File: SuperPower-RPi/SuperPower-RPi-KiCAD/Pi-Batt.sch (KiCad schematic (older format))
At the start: 10 parts, among them J2 Conn_01x02, J4 Conn_01x02, Q1 SSM3J328R, Q6 Q_NMOS_GSD

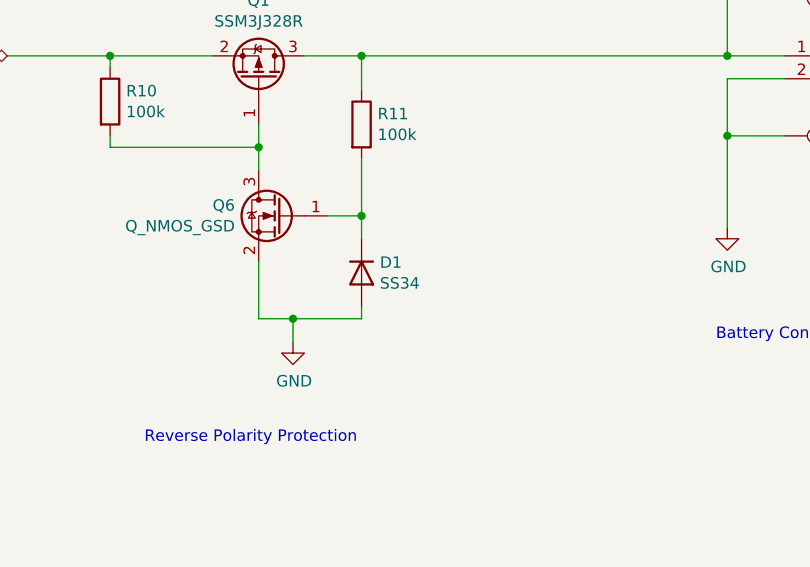
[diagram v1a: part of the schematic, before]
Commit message: Shrank Components and seleected NMOS part.
Shrank diodes to SOD523 and 100k resistors to 0402.
Selected 2N7002 for generic NMOS.
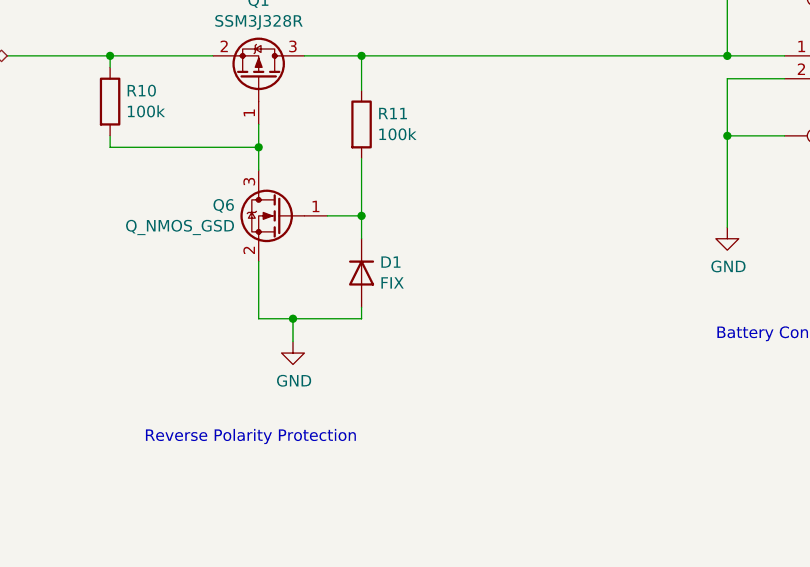
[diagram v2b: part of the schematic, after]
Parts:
- D1: value SS34 -> FIX; footprint Diode_SMD:D_SOD-123 -> Diode_SMD:D_SOD-523
- R10, R11: footprint Resistor_SMD:R_0603_1608Metric -> Resistor_SMD:R_0402_1005Metric; Digi-Key PN 311-100KHRCT-ND -> (none); Mfg Yageo -> (none); Mfg PN RC0603FR-07100KL -> (none)
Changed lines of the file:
@@
 P 6100 3350
 F 0 "D1" V 6054 3430 50  0000 L CNN
-F 1 "SS34" V 6145 3430 50  0000 L CNN
-F 2 "Diode_SMD:D_SOD-123" H 6100 3350 50  0001 C CNN
+F 1 "FIX" V 6145 3430 50  0000 L CNN
+F 2 "Diode_SMD:D_SOD-523" H 6100 3350 50  0001 C CNN
 F 3 "~" H 6100 3350 50  0001 C CNN
 F 4 "FIX FOOTPRINT" H 6100 3350 50  0001 C CNN "Mfg"
@@
 F 0 "R11" H 6170 2746 50  0000 L CNN
 F 1 "100k" H 6170 2655 50  0000 L CNN
-F 2 "Resistor_SMD:R_0603_1608Metric" V 6030 2700 50  0001 C CNN
+F 2 "Resistor_SMD:R_0402_1005Metric" V 6030 2700 50  0001 C CNN
 F 3 "~" H 6100 2700 50  0001 C CNN
-F 4 "311-100KHRCT-ND" H 6100 2700 50  0001 C CNN "Digi-Key PN"
-F 5 "Yageo" H 6100 2700 50  0001 C CNN "Mfg"
-F 6 "RC0603FR-07100KL" H 6100 2700 50  0001 C CNN "Mfg PN"
+F 4 "" H 6100 2700 50  0001 C CNN "Digi-Key PN"
+F 5 "" H 6100 2700 50  0001 C CNN "Mfg"
+F 6 "" H 6100 2700 50  0001 C CNN "Mfg PN"
 	1    6100 2700
 	1    0    0    -1
@@
 F 0 "R10" H 5070 2646 50  0000 L CNN
 F 1 "100k" H 5070 2555 50  0000 L CNN
-F 2 "Resistor_SMD:R_0603_1608Metric" V 4930 2600 50  0001 C CNN
+F 2 "Resistor_SMD:R_0402_1005Metric" V 4930 2600 50  0001 C CNN
 F 3 "~" H 5000 2600 50  0001 C CNN
-F 4 "311-100KHRCT-ND" H 5000 2600 50  0001 C CNN "Digi-Key PN"
-F 5 "Yageo" H 5000 2600 50  0001 C CNN "Mfg"
-F 6 "RC0603FR-07100KL" H 5000 2600 50  0001 C CNN "Mfg PN"
+F 4 "" H 5000 2600 50  0001 C CNN "Digi-Key PN"
+F 5 "" H 5000 2600 50  0001 C CNN "Mfg"
+F 6 "" H 5000 2600 50  0001 C CNN "Mfg PN"
 	1    5000 2600
 	1    0    0    -1

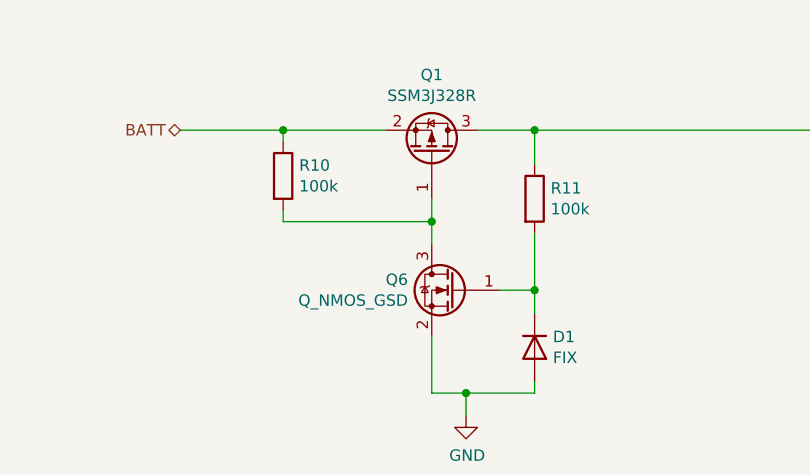
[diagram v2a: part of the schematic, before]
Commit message: Updated Component Meta-data
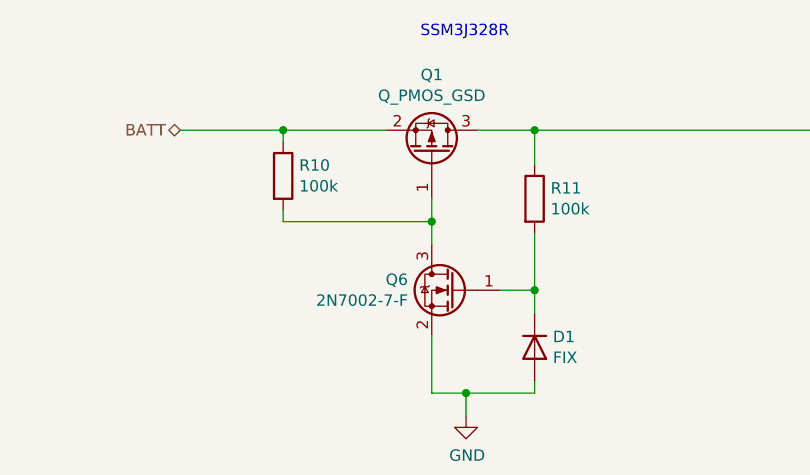
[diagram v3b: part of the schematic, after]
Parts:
- Q1: value SSM3J328R -> Q_PMOS_GSD
- Q6: value Q_NMOS_GSD -> 2N7002-7-F; Digi-Key PN (none) -> 2N7002-FDICT-ND; Mfg FIX FOOTPRINT -> Diodes Incorporated; Mfg PN (none) -> 2N7002-7-F
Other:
- note added: "SSM3J328R"
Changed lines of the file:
@@
 P 5650 2500
 F 0 "Q1" V 5992 2500 50  0000 C CNN
-F 1 "SSM3J328R" V 5901 2500 50  0000 C CNN
+F 1 "Q_PMOS_GSD" V 5901 2500 50  0000 C CNN
 F 2 "Package_TO_SOT_SMD:SOT-23" H 5850 2600 50  0001 C CNN
 F 3 "~" H 5650 2500 50  0001 C CNN
@@
 AR Path="/5F6AC644/5FA86C0C" Ref="Q6"  Part="1"
 F 0 "Q6" H 5954 3146 50  0000 L CNN
-F 1 "Q_NMOS_GSD" H 5954 3055 50  0000 L CNN
+F 1 "2N7002-7-F" H 5954 3055 50  0000 L CNN
 F 2 "Package_TO_SOT_SMD:SOT-23" H 5950 3200 50  0001 C CNN
 F 3 "~" H 5750 3100 50  0001 C CNN
-F 4 "FIX FOOTPRINT" H 5750 3100 50  0001 C CNN "Mfg"
+F 4 "Diodes Incorporated" H 5750 3100 50  0001 C CNN "Mfg"
+F 5 "2N7002-FDICT-ND" H 5750 3100 50  0001 C CNN "Digi-Key PN"
+F 6 "2N7002-7-F" H 5750 3100 50  0001 C CNN "Mfg PN"
 	1    5750 3100
 	-1   0    0    -1
@@
 Wire Wire Line
 	4100 6250 4100 6000
+Text Notes 5600 2000 0    50   ~ 0
+SSM3J328R
 $EndSCHEMATC

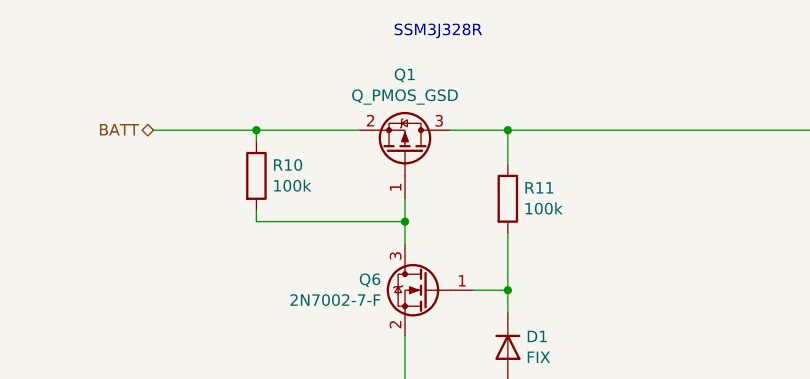
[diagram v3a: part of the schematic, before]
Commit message: Selected part for PMOS: DMP3056.
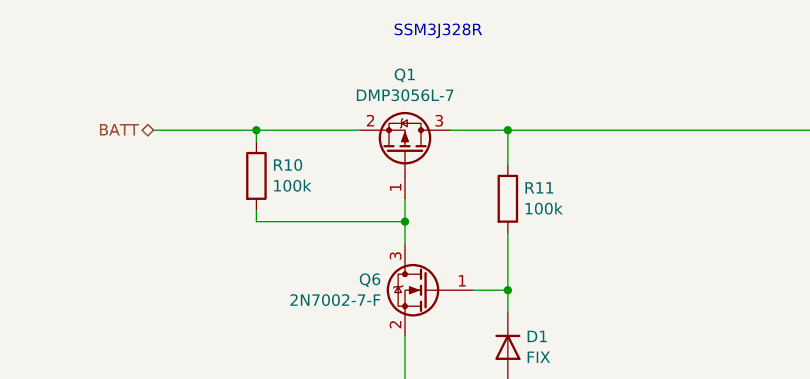
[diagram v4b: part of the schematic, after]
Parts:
- removed Q1: Q_PMOS_GSD, Package_TO_SOT_SMD:SOT-23, symbol Device:Q_PMOS_GSD
- added Q1: Q_PMOS_DMP3056L-7_SOT-23, Package_TO_SOT_SMD:SOT-23, symbol Manual_Lib:Q_PMOS_DMP3056L-7_SOT-23
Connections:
- net BATT: now also Q1.2 (S)
- net at J2.1 (Pin_1), R11.1, TP1.1: now also Q1.3 (D)
- net at Q6.3 (D), R10.2: now also Q1.1 (G)
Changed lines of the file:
@@
 	1    0    0    -1
-$EndComp
-$Comp
-L Device:Q_PMOS_GSD Q1
-U 1 1 5F704F9B
-P 5650 2500
-F 0 "Q1" V 5992 2500 50  0000 C CNN
-F 1 "Q_PMOS_GSD" V 5901 2500 50  0000 C CNN
-F 2 "Package_TO_SOT_SMD:SOT-23" H 5850 2600 50  0001 C CNN
-F 3 "~" H 5650 2500 50  0001 C CNN
-F 4 "FIX FOOTPRINT" H 5650 2500 50  0001 C CNN "Mfg"
-	1    5650 2500
-	0    1    -1   0
 $EndComp
 Wire Wire Line
@@
 Text Notes 5600 2000 0    50   ~ 0
 SSM3J328R
+$Comp
+L Manual_Lib:Q_PMOS_DMP3056L-7_SOT-23 Q1
+U 1 1 5FCC9BCC
+P 5650 2500
+F 0 "Q1" V 5992 2500 50  0000 C CNN
+F 1 "Q_PMOS_DMP3056L-7_SOT-23" H 5850 2450 50  0001 L CNN
+F 2 "Package_TO_SOT_SMD:SOT-23" H 5850 2600 50  0001 C CNN
+F 3 "https://www.diodes.com/assets/Datasheets/DMP3056L.pdf" H 5650 2500 50  0001 C CNN
+F 4 "Diodes Incorporated" H 5650 2500 50  0001 C CNN "Mfg"
+F 5 "DMP3056L-7" V 5901 2500 50  0000 C CNN "Mfg PN"
+F 6 "DMP3056L-7DICT-ND" H 5650 2500 50  0001 C CNN "Digi-Key PN"
+	1    5650 2500
+	0    1    -1   0
+$EndComp
 $EndSCHEMATC

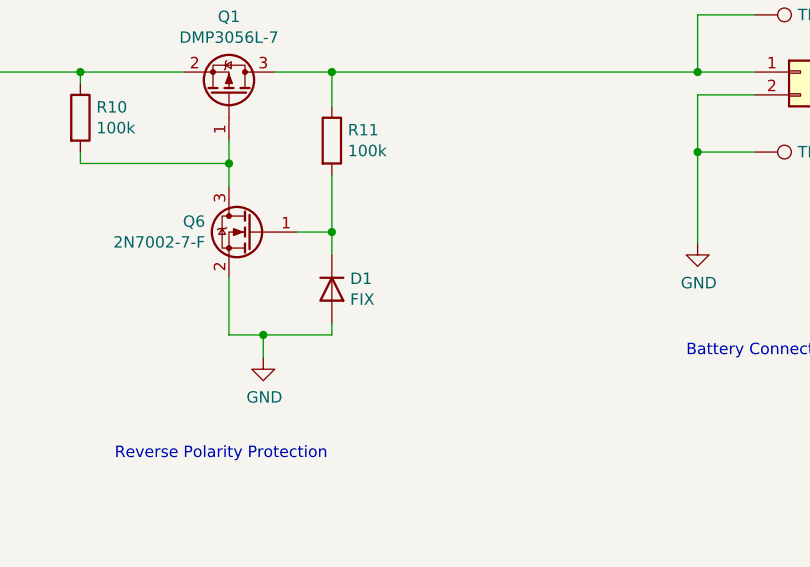
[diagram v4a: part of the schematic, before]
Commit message: Chose component for Zener Diode and imported into PCB.
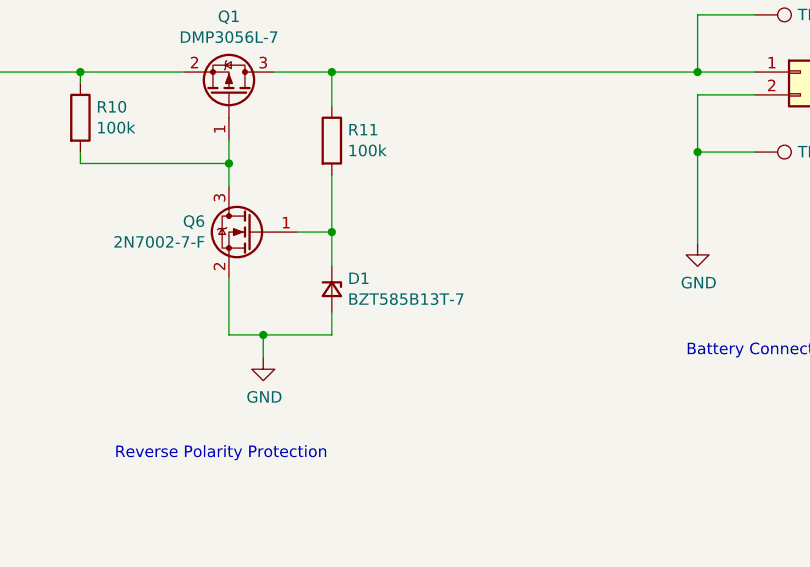
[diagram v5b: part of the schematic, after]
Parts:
- removed D1: FIX, Diode_SMD:D_SOD-523, symbol Device:D
- added D1: BZT585B13T-7, Diode_SMD:D_SOD-523, symbol Device:D_Zener_Small
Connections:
- net GND: now also D1.2 (A)
- net at Q6.1 (G), R11.2: now also D1.1 (K)
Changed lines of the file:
@@
-$EndComp
-$Comp
-L Device:D D1
-U 1 1 5F702A8B
-P 6100 3350
-F 0 "D1" V 6054 3430 50  0000 L CNN
-F 1 "FIX" V 6145 3430 50  0000 L CNN
-F 2 "Diode_SMD:D_SOD-523" H 6100 3350 50  0001 C CNN
-F 3 "~" H 6100 3350 50  0001 C CNN
-F 4 "FIX FOOTPRINT" H 6100 3350 50  0001 C CNN "Mfg"
-	1    6100 3350
-	0    1    1    0
 $EndComp
 $Comp
@@
 Wire Wire Line
 	5650 3550 5800 3550
-Wire Wire Line
-	6100 3550 6100 3500
-Wire Wire Line
-	6100 3200 6100 3100
 Wire Wire Line
 	5950 3100 6100 3100
@@
 	0    1    -1   0
 $EndComp
+$Comp
+L Device:D_Zener_Small D?
+U 1 1 5FCD8B27
+P 6100 3350
+AR Path="/5F6AC66E/5FCD8B27" Ref="D?"  Part="1"
+AR Path="/5F6AC644/5FCD8B27" Ref="D1"  Part="1"
+F 0 "D1" V 6054 3420 50  0000 L CNN
+F 1 "BZT585B13T-7" V 6145 3420 50  0000 L CNN
+F 2 "Diode_SMD:D_SOD-523" V 6100 3350 50  0001 C CNN
+F 3 "https://www.diodes.com/assets/Datasheets/BZT585BxVxT.pdf" V 6100 3350 50  0001 C CNN
+F 4 "Diodes Incorporated" H 6100 3350 50  0001 C CNN "Mfg"
+F 5 "BZT585B13T-7" H 6100 3350 50  0001 C CNN "Mfg PN"
+F 6 "BZT585B13T-7DICT-ND" H 6100 3350 50  0001 C CNN "Digi-Key PN"
+	1    6100 3350
+	0    1    1    0
+$EndComp
+Wire Wire Line
+	6100 3450 6100 3550
+Wire Wire Line
+	6100 3100 6100 3250
 $EndSCHEMATC

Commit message: Updated meta-data.
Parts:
- R22, TP1, TP2: Mfg (none) -> DNP
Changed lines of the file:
@@
 F 2 "Connector_Wire:SolderWire-1.5sqmm_1x01_D1.7mm_OD3.9mm" H 8150 2750 50  0001 C CNN
 F 3 "~" H 8150 2750 50  0001 C CNN
+F 4 "DNP" H 7950 2750 50  0001 C CNN "Mfg"
 	1    7950 2750
 	0    1    1    0
@@
 F 2 "Connector_Wire:SolderWire-1.5sqmm_1x01_D1.7mm_OD3.9mm" H 8150 2150 50  0001 C CNN
 F 3 "~" H 8150 2150 50  0001 C CNN
+F 4 "DNP" H 7950 2150 50  0001 C CNN "Mfg"
 	1    7950 2150
 	0    1    1    0
@@
 F 2 "Resistor_SMD:R_0603_1608Metric" H 3900 6100 50  0001 C CNN
 F 3 "~" H 3900 6100 50  0001 C CNN
+F 4 "DNP" H 3900 6100 50  0001 C CNN "Mfg"
 	1    3900 6100
 	1    0    0    1

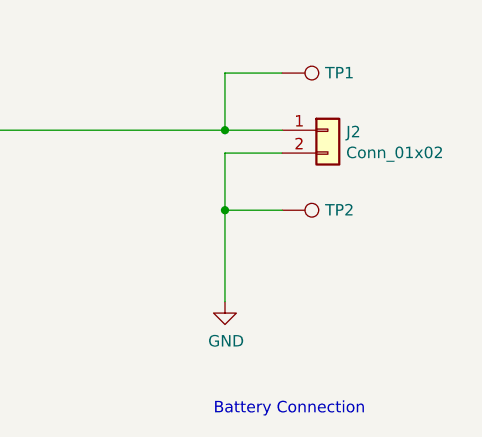
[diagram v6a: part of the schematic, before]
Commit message: Changed Battery Connector to Side Entry Type JST-PH.
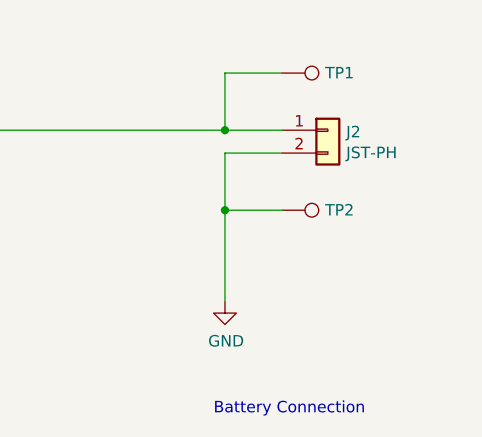
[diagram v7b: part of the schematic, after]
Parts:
- J2: value Conn_01x02 -> JST-PH; footprint Connector_JST:JST_PH_B2B-PH-K_1x02_P2.00mm_Vertical -> Connector_JST:JST_PH_S2B-PH-K_1x02_P2.00mm_Horizontal; Mfg FIX FOOTPRINT -> (none)
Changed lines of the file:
@@
 P 8150 2400
 F 0 "J2" H 8230 2392 50  0000 L CNN
-F 1 "Conn_01x02" H 8230 2301 50  0000 L CNN
-F 2 "Connector_JST:JST_PH_B2B-PH-K_1x02_P2.00mm_Vertical" H 8150 2400 50  0001 C CNN
+F 1 "JST-PH" H 8230 2301 50  0000 L CNN
+F 2 "Connector_JST:JST_PH_S2B-PH-K_1x02_P2.00mm_Horizontal" H 8150 2400 50  0001 C CNN
 F 3 "~" H 8150 2400 50  0001 C CNN
-F 4 "FIX FOOTPRINT" H 8150 2400 50  0001 C CNN "Mfg"
 	1    8150 2400
 	1    0    0    -1

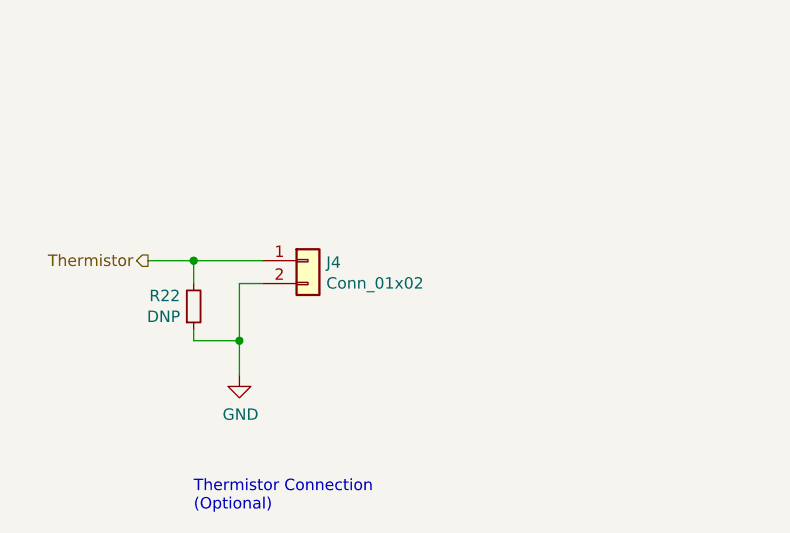
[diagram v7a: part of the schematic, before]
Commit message: Updated schematic to fill out all BOM entries.
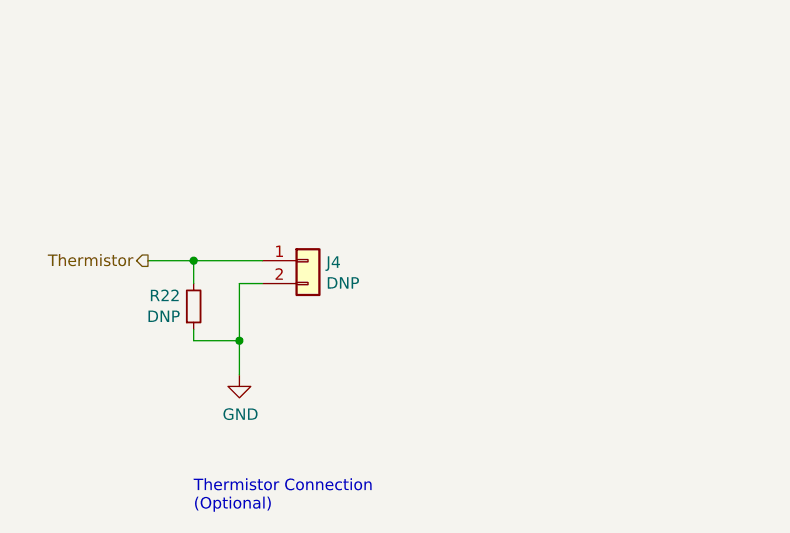
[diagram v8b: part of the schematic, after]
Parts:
- J2: Mfg (none) -> JST; Mfg PN (none) -> S2B-PH-K-S(LF)(SN)
- J4: value Conn_01x02 -> DNP; Mfg (none) -> DNP; Mfg PN (none) -> DNP
- R10, R11: Digi-Key PN (none) -> 311-100KLRCT-ND; Mfg (none) -> Yageo; Mfg PN (none) -> RC0402FR-07100KL
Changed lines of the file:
@@
 F 2 "Connector_JST:JST_PH_S2B-PH-K_1x02_P2.00mm_Horizontal" H 8150 2400 50  0001 C CNN
 F 3 "~" H 8150 2400 50  0001 C CNN
+F 4 "JST" H 8150 2400 50  0001 C CNN "Mfg"
+F 5 "S2B-PH-K-S(LF)(SN)" H 8150 2400 50  0001 C CNN "Mfg PN"
 	1    8150 2400
 	1    0    0    -1
@@
 F 2 "Resistor_SMD:R_0402_1005Metric" V 6030 2700 50  0001 C CNN
 F 3 "~" H 6100 2700 50  0001 C CNN
-F 4 "" H 6100 2700 50  0001 C CNN "Digi-Key PN"
-F 5 "" H 6100 2700 50  0001 C CNN "Mfg"
-F 6 "" H 6100 2700 50  0001 C CNN "Mfg PN"
+F 4 "311-100KLRCT-ND" H 6100 2700 50  0001 C CNN "Digi-Key PN"
+F 5 "Yageo" H 6100 2700 50  0001 C CNN "Mfg"
+F 6 "RC0402FR-07100KL" H 6100 2700 50  0001 C CNN "Mfg PN"
 	1    6100 2700
 	1    0    0    -1
@@
 F 2 "Resistor_SMD:R_0402_1005Metric" V 4930 2600 50  0001 C CNN
 F 3 "~" H 5000 2600 50  0001 C CNN
-F 4 "" H 5000 2600 50  0001 C CNN "Digi-Key PN"
-F 5 "" H 5000 2600 50  0001 C CNN "Mfg"
-F 6 "" H 5000 2600 50  0001 C CNN "Mfg PN"
+F 4 "311-100KLRCT-ND" H 5000 2600 50  0001 C CNN "Digi-Key PN"
+F 5 "Yageo" H 5000 2600 50  0001 C CNN "Mfg"
+F 6 "RC0402FR-07100KL" H 5000 2600 50  0001 C CNN "Mfg PN"
 	1    5000 2600
 	1    0    0    -1
@@
 P 4400 5900
 F 0 "J4" H 4480 5892 50  0000 L CNN
-F 1 "Conn_01x02" H 4480 5801 50  0000 L CNN
+F 1 "DNP" H 4480 5801 50  0000 L CNN
 F 2 "Connector_PinHeader_2.00mm:PinHeader_1x02_P2.00mm_Vertical" H 4400 5900 50  0001 C CNN
 F 3 "~" H 4400 5900 50  0001 C CNN
+F 4 "DNP" H 4400 5900 50  0001 C CNN "Mfg"
+F 5 "DNP" H 4400 5900 50  0001 C CNN "Mfg PN"
 	1    4400 5900
 	1    0    0    -1
